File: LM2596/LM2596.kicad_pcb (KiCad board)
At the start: 2 copper layers, 5 parts, among them U1 LM2596S-5

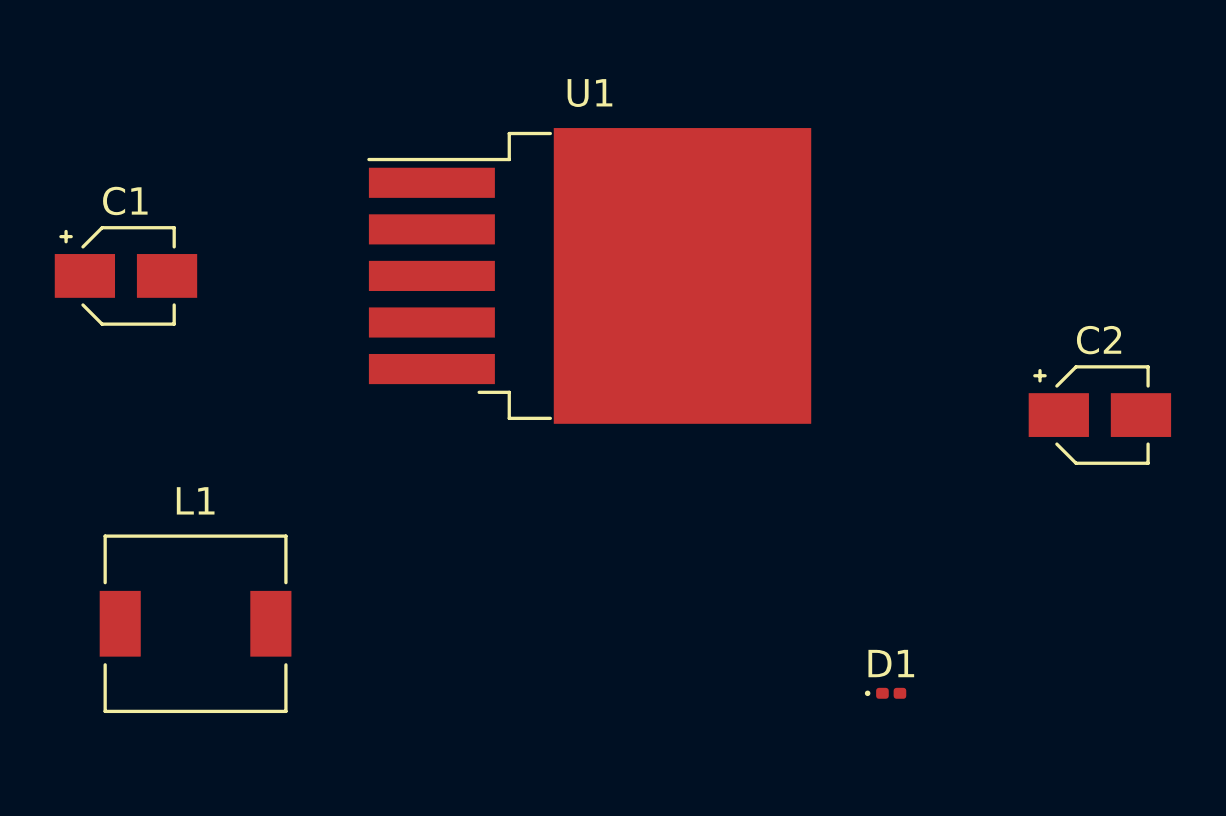
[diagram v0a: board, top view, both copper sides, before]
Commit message: 13/10/2022
Sistemato lo schema elettrico.
Creato le tracce nel file PCB.
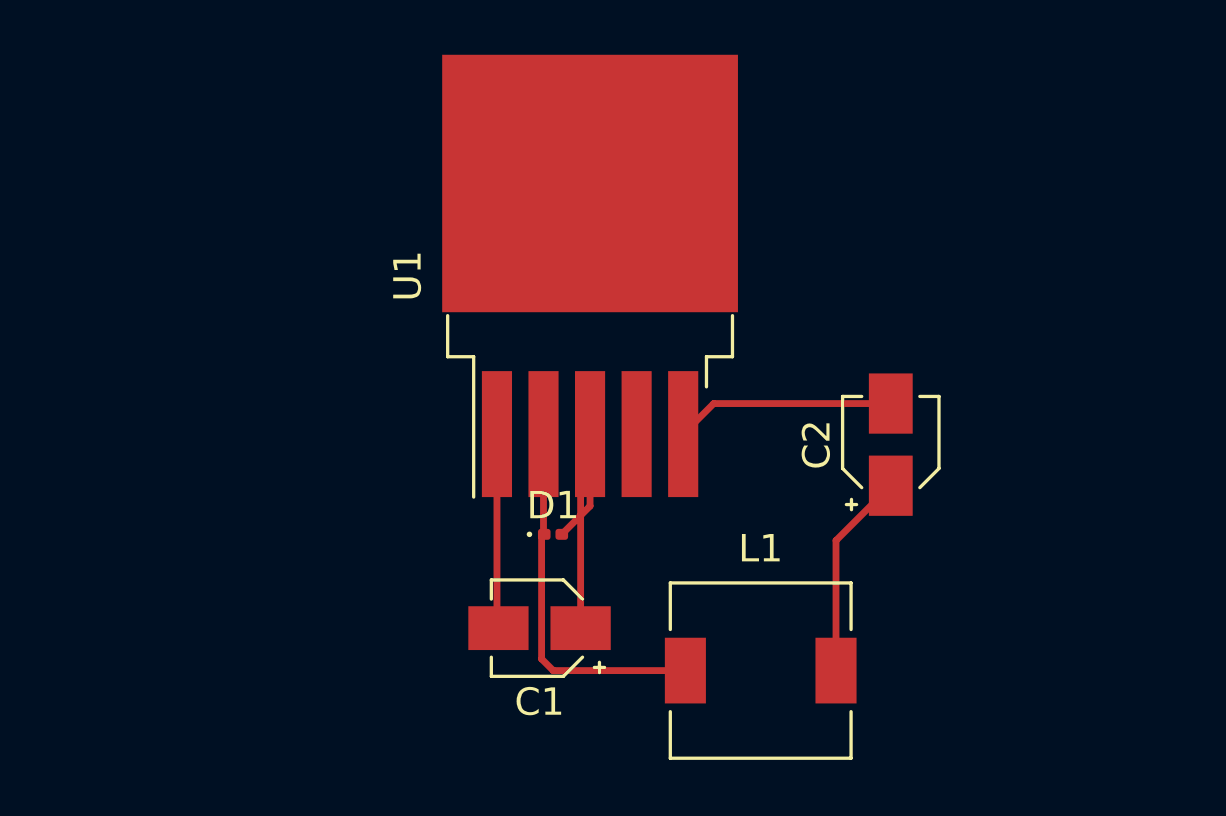
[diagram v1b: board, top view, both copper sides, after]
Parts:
- moved L1 20.7 mm to (162.9, 55.0)
- moved C1 19.8 mm to (154.8, 53.5), turned to 180 degrees
- moved D1 13.6 mm to (155.3, 50.1)
- moved C2 7.71 mm to (167.6, 46.8), turned to 90 degrees
- turned U1 to 90 degrees
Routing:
- net GND: track 0.00 -> 19.4 mm
- net Net-(D1-Pad1): track 0.00 -> 13.7 mm
- net 5v: track 0.00 -> 9.41 mm
- net Net-(C1-Pad2): track 0.00 -> 7.11 mm
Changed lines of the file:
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@@
   (net 4 "Net-(D1-Pad1)")
   (footprint "Inductor_SMD:L_6.3x6.3_H3" (layer "F.Cu")
-    (at 142.24 53.34)
+    (at 162.875 55.05)
     (descr "Choke, SMD, 6.3x6.3mm 3mm height")
     (tags "Choke SMD")
@@
   )
   (footprint "Package_TO_SOT_SMD:TO-263-5_TabPin3" (layer "F.Cu")
-    (at 156.645 40.64)
+    (at 156.645 40.64 90)
     (descr "TO-263 / D2PAK / DDPAK SMD package, http://www.infineon.com/cms/en/product/packages/PG-TO263/PG-TO263-5-1/")
     (tags "D2PAK DDPAK TO-263 D2PAK-5 TO-263-5 SOT-426")
@@
     (property "Sheetname" "")
     (attr smd)
-    (fp_text reference "U1" (at 0 -6.65) (layer "F.SilkS")
-      (effects (font (size 1 1) (thickness 0.15)))
-    )
-    (fp_text value "LM2596S-5" (at 0 6.65) (layer "F.Fab")
-      (effects (font (size 1 1) (thickness 0.15)))
-    )
-    (fp_text user "${REFERENCE}" (at 0 0) (layer "F.Fab")
+    (fp_text reference "U1" (at 0 -6.65 90) (layer "F.SilkS")
+      (effects (font (size 1 1) (thickness 0.15)))
+    )
+    (fp_text value "LM2596S-5" (at 0 6.65 90) (layer "F.Fab")
+      (effects (font (size 1 1) (thickness 0.15)))
+    )
+    (fp_text user "${REFERENCE}" (at 0 0 90) (layer "F.Fab")
       (effects (font (size 1 1) (thickness 0.15)))
     )
@@
     (fp_line (start -7.45 0.4) (end -2.75 0.4) (layer "F.Fab") (width 0.1))
     (fp_line (start -7.45 -1.3) (end -2.75 -1.3) (layer "F.Fab") (width 0.1))
-    (pad "" smd rect (at 5.8 2.775) (size 4.55 5.25) (layers "F.Paste"))
-    (pad "" smd rect (at 0.95 2.775) (size 4.55 5.25) (layers "F.Paste"))
-    (pad "" smd rect (at 5.8 -2.775) (size 4.55 5.25) (layers "F.Paste"))
-    (pad "" smd rect (at 0.95 -2.775) (size 4.55 5.25) (layers "F.Paste"))
-    (pad "1" smd rect (at -5.775 -3.4) (size 4.6 1.1) (layers "F.Cu" "F.Paste" "F.Mask")
+    (pad "" smd rect (at 5.8 2.775 90) (size 4.55 5.25) (layers "F.Paste"))
+    (pad "" smd rect (at 0.95 2.775 90) (size 4.55 5.25) (layers "F.Paste"))
+    (pad "" smd rect (at 5.8 -2.775 90) (size 4.55 5.25) (layers "F.Paste"))
+    (pad "" smd rect (at 0.95 -2.775 90) (size 4.55 5.25) (layers "F.Paste"))
+    (pad "1" smd rect (at -5.775 -3.4 90) (size 4.6 1.1) (layers "F.Cu" "F.Paste" "F.Mask")
       (net 2 "Net-(C1-Pad2)") (pinfunction "VIN") (pintype "power_in"))
-    (pad "2" smd rect (at -5.775 -1.7) (size 4.6 1.1) (layers "F.Cu" "F.Paste" "F.Mask")
+    (pad "2" smd rect (at -5.775 -1.7 90) (size 4.6 1.1) (layers "F.Cu" "F.Paste" "F.Mask")
       (net 4 "Net-(D1-Pad1)") (pinfunction "OUT") (pintype "output"))
-    (pad "3" smd rect (at 3.375 0) (size 9.4 10.8) (layers "F.Cu" "F.Mask")
+    (pad "3" smd rect (at 3.375 0 90) (size 9.4 10.8) (layers "F.Cu" "F.Mask")
       (net 1 "GND") (pinfunction "GND") (pintype "power_in"))
-    (pad "3" smd rect (at -5.775 0) (size 4.6 1.1) (layers "F.Cu" "F.Paste" "F.Mask")
+    (pad "3" smd rect (at -5.775 0 90) (size 4.6 1.1) (layers "F.Cu" "F.Paste" "F.Mask")
       (net 1 "GND") (pinfunction "GND") (pintype "power_in"))
-    (pad "4" smd rect (at -5.775 1.7) (size 4.6 1.1) (layers "F.Cu" "F.Paste" "F.Mask")
+    (pad "4" smd rect (at -5.775 1.7 90) (size 4.6 1.1) (layers "F.Cu" "F.Paste" "F.Mask")
       (net 3 "5v") (pinfunction "FB") (pintype "input"))
-    (pad "5" smd rect (at -5.775 3.4) (size 4.6 1.1) (layers "F.Cu" "F.Paste" "F.Mask")
+    (pad "5" smd rect (at -5.775 3.4 90) (size 4.6 1.1) (layers "F.Cu" "F.Paste" "F.Mask")
       (net 1 "GND") (pinfunction "~{ON}/OFF") (pintype "input"))
     (model "${KICAD6_3DMODEL_DIR}/Package_TO_SOT_SMD.3dshapes/TO-263-5_TabPin3.wrl"
@@
   )
   (footprint "Capacitor_SMD:CP_Elec_3x5.3" (layer "F.Cu")
-    (at 175.26 45.72)
+    (at 167.625 46.8 90)
     (descr "SMT capacitor, aluminium electrolytic, 3x5.3, Cornell Dubilier Electronics ")
     (tags "Capacitor Electrolytic")
@@
     (property "Sheetname" "")
     (attr smd)
-    (fp_text reference "C2" (at 0 -2.7) (layer "F.SilkS")
-      (effects (font (size 1 1) (thickness 0.15)))
-    )
-    (fp_text value "220uF" (at 0 2.7) (layer "F.Fab")
-      (effects (font (size 1 1) (thickness 0.15)))
-    )
-    (fp_text user "${REFERENCE}" (at 0 0) (layer "F.Fab")
+    (fp_text reference "C2" (at 0 -2.7 90) (layer "F.SilkS")
+      (effects (font (size 1 1) (thickness 0.15)))
+    )
+    (fp_text value "220uF" (at 0 2.7 90) (layer "F.Fab")
+      (effects (font (size 1 1) (thickness 0.15)))
+    )
+    (fp_text user "${REFERENCE}" (at 0 0 90) (layer "F.Fab")
       (effects (font (size 0.6 0.6) (thickness 0.09)))
     )
@@
     (fp_line (start 1.65 -1.65) (end 1.65 1.65) (layer "F.Fab") (width 0.1))
     (fp_circle (center 0 0) (end 1.5 0) (layer "F.Fab") (width 0.1) (fill none))
-    (pad "1" smd rect (at -1.5 0) (size 2.2 1.6) (layers "F.Cu" "F.Paste" "F.Mask")
+    (pad "1" smd rect (at -1.5 0 90) (size 2.2 1.6) (layers "F.Cu" "F.Paste" "F.Mask")
       (net 3 "5v") (pintype "passive"))
-    (pad "2" smd rect (at 1.5 0) (size 2.2 1.6) (layers "F.Cu" "F.Paste" "F.Mask")
+    (pad "2" smd rect (at 1.5 0 90) (size 2.2 1.6) (layers "F.Cu" "F.Paste" "F.Mask")
       (net 1 "GND") (pintype "passive"))
     (model "${KICAD6_3DMODEL_DIR}/Capacitor_SMD.3dshapes/CP_Elec_3x5.3.wrl"
@@
   )
   (footprint "Capacitor_SMD:CP_Elec_3x5.3" (layer "F.Cu")
-    (at 139.7 40.64)
+    (at 154.8 53.5 180)
     (descr "SMT capacitor, aluminium electrolytic, 3x5.3, Cornell Dubilier Electronics ")
     (tags "Capacitor Electrolytic")
@@
     (fp_line (start -0.825 1.65) (end 1.65 1.65) (layer "F.Fab") (width 0.1))
     (fp_circle (center 0 0) (end 1.5 0) (layer "F.Fab") (width 0.1) (fill none))
-    (pad "1" smd rect (at -1.5 0) (size 2.2 1.6) (layers "F.Cu" "F.Paste" "F.Mask")
+    (pad "1" smd rect (at -1.5 0 180) (size 2.2 1.6) (layers "F.Cu" "F.Paste" "F.Mask")
       (net 1 "GND") (pintype "passive"))
-    (pad "2" smd rect (at 1.5 0) (size 2.2 1.6) (layers "F.Cu" "F.Paste" "F.Mask")
+    (pad "2" smd rect (at 1.5 0 180) (size 2.2 1.6) (layers "F.Cu" "F.Paste" "F.Mask")
       (net 2 "Net-(C1-Pad2)") (pintype "passive"))
     (model "${KICAD6_3DMODEL_DIR}/Capacitor_SMD.3dshapes/CP_Elec_3x5.3.wrl"
@@
   )
   (footprint "Diode_SMD:D_0201_0603Metric" (layer "F.Cu")
-    (at 167.64 55.88)
+    (at 155.2925 50.075)
     (descr "Diode SMD 0201 (0603 Metric), square (rectangular) end terminal, IPC_7351 nominal, (Body size source: https://www.vishay.com/docs/20052/crcw0201e3.pdf), generated with kicad-footprint-generator")
     (tags "diode")
@@
     )
   )
+  (segment (start 156.645 49.0425) (end 156.645 46.415) (width 0.25) (layer "F.Cu") (net 1))
+  (segment (start 156.3 53.5) (end 156.3 46.76) (width 0.25) (layer "F.Cu") (net 1))
+  (segment (start 161.16 45.3) (end 160.045 46.415) (width 0.25) (layer "F.Cu") (net 1))
+  (segment (start 167.625 45.3) (end 161.16 45.3) (width 0.25) (layer "F.Cu") (net 1))
+  (segment (start 156.3 46.76) (end 156.645 46.415) (width 0.25) (layer "F.Cu") (net 1))
+  (segment (start 155.6125 50.075) (end 156.645 49.0425) (width 0.25) (layer "F.Cu") (net 1))
+  (segment (start 153.245 53.445) (end 153.3 53.5) (width 0.25) (layer "F.Cu") (net 2))
+  (segment (start 153.245 46.415) (end 153.245 53.445) (width 0.25) (layer "F.Cu") (net 2))
+  (segment (start 165.625 55.05) (end 165.625 50.3) (width 0.25) (layer "F.Cu") (net 3))
+  (segment (start 165.625 50.3) (end 167.625 48.3) (width 0.25) (layer "F.Cu") (net 3))
+  (segment (start 158.345 48.245) (end 158.345 46.415) (width 0.25) (layer "F.Cu") (net 3))
+  (segment (start 154.875 50.1725) (end 154.9725 50.075) (width 0.25) (layer "F.Cu") (net 4))
+  (segment (start 154.875 54.625) (end 154.875 50.1725) (width 0.25) (layer "F.Cu") (net 4))
+  (segment (start 155.3 55.05) (end 154.875 54.625) (width 0.25) (layer "F.Cu") (net 4))
+  (segment (start 160.125 55.05) (end 155.3 55.05) (width 0.25) (layer "F.Cu") (net 4))
+  (segment (start 154.945 46.415) (end 154.945 50.0475) (width 0.25) (layer "F.Cu") (net 4))
+  (segment (start 154.945 50.0475) (end 154.9725 50.075) (width 0.25) (layer "F.Cu") (net 4))
 )
